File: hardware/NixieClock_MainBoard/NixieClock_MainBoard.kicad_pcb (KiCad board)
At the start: 2 copper layers, 152.4 x 63.5 mm, 107 parts, among them J1 Conn_01x14, J10 Conn_01x04, J11 Conn_01x04, J12 Conn_01x03, J13 Conn_01x03, J2 Conn_01x08, J3 Conn_01x08, J4 Conn_01x08, J5 Conn_01x08, J6 USB_C_Receptacle_USB2.0_16P, J7 Micro_SD_Card, J8 Conn_01x08, J9 Conn_01x03, Q1 BC847, Q2 BC847, Q3 BSS123, Q4 Si2319CDS, U1 ESP32-WROOM-32E, U10 NC7SZ125M5X, U12 NC7SZ125M5X, U13 NC7SZ125M5X, U14 CP2102N-Axx-xQFN24, U15 CH340C, U16 NC7SZ125M5X, U17 NC7SZ125M5X, U18 NC7SZ125M5X, U19 NC7SZ125M5X, U2 R-78C3.3-1.0, U20 NC7SZ125M5X, U21 NC7SZ125M5X, U3 NC7SZ125M5X, U4 PCA9635, U5 NC7SZ125M5X, U6 PCA9538A, U7 NC7SZ125M5X, U8 NC7SZ125M5X, U9 NC7SZ125M5X

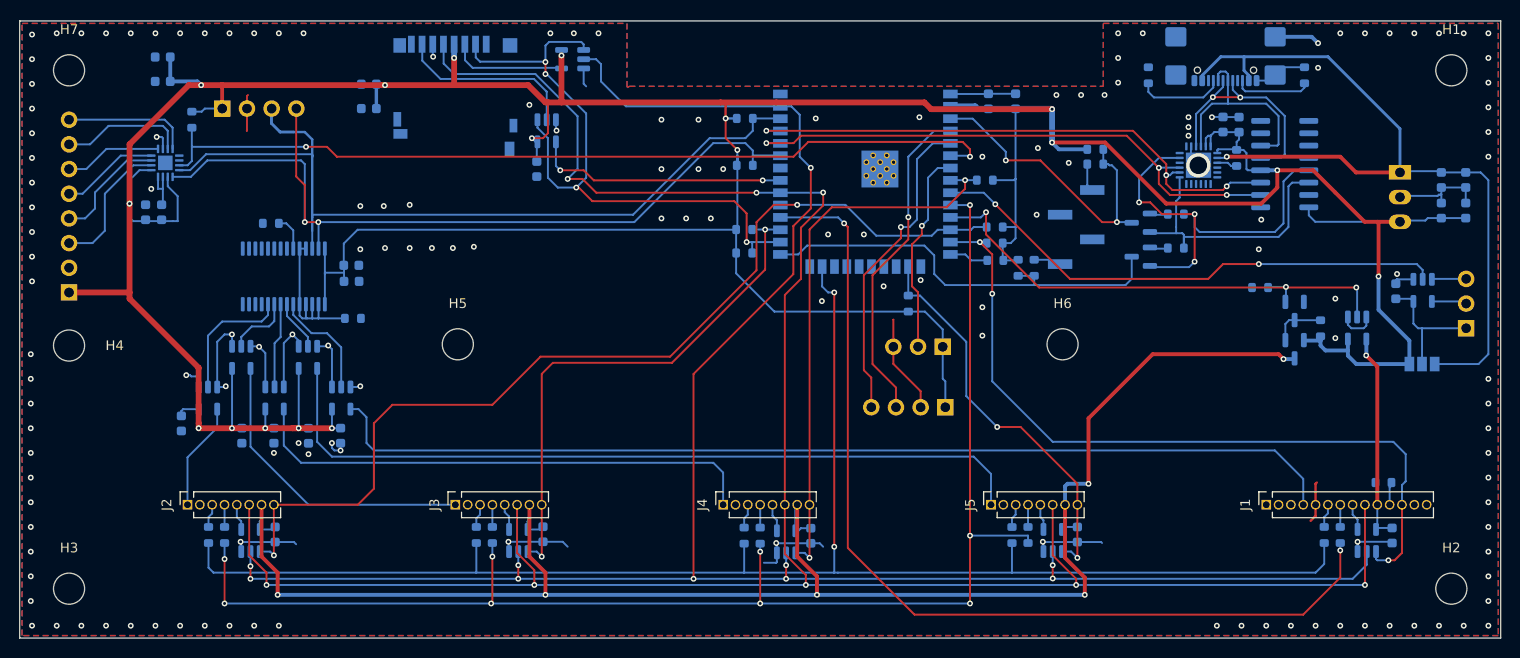
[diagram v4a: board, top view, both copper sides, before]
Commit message: Hardware V2.1 add NixieClock_MainBoard/NixieClock_Schematic.pdf
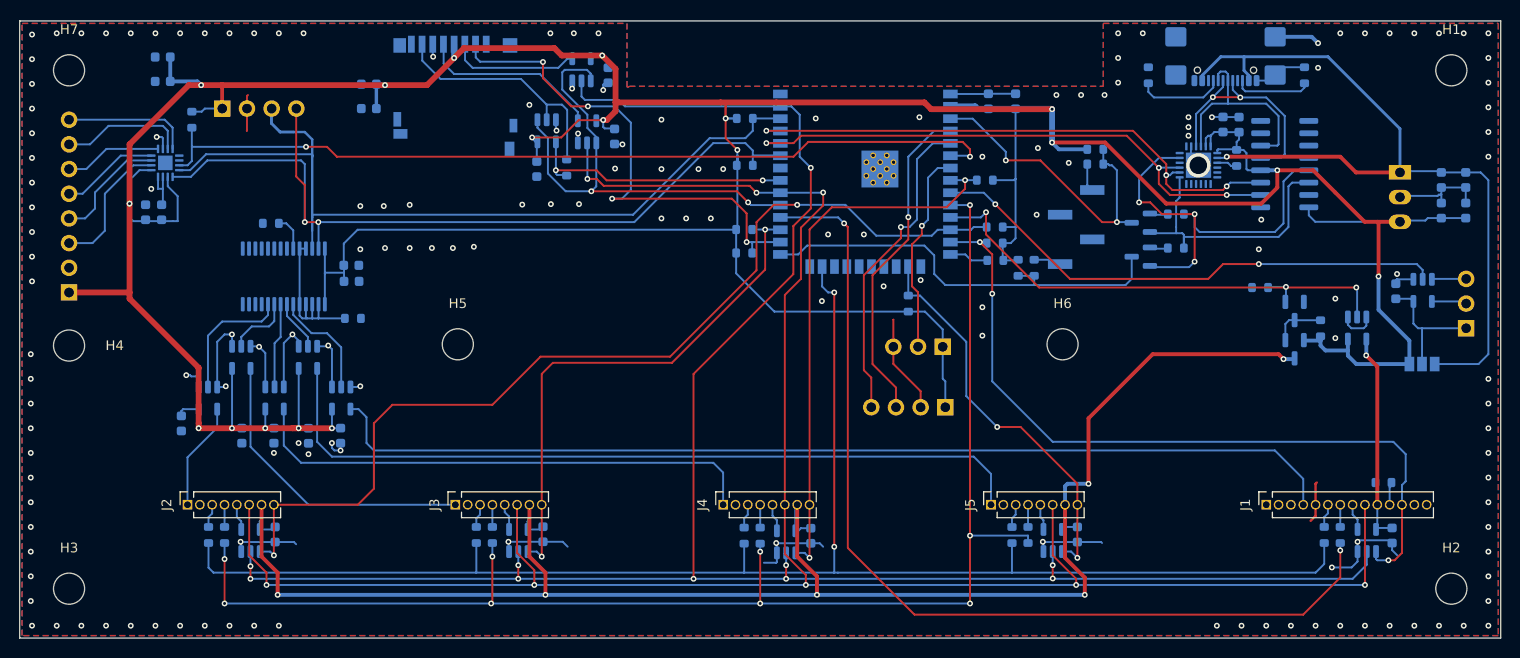
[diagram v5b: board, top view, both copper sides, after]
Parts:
- added C29: 100nF, Capacitor_SMD:C_0603_1608Metric, B.Cu at (98.7, 81.8)
- added C30: 100nF, Capacitor_SMD:C_0603_1608Metric, B.Cu at (99.3, 88.1)
- added R35: R, Resistor_SMD:R_0603_1608Metric, B.Cu at (94.4, 91.3)
- added U11: NC7SZ125M5X, Package_TO_SOT_SMD:SOT-23-5, B.Cu at (96.5, 87.6)
- moved U20 1.42 mm to (95.9, 81.2), turned to 90 degrees
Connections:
- J7 pad 5: /SCLK -> Net-(J7-CLK)
- U1 pad 29: unconnected-(U1-IO5-Pad29) -> /OE_MEM
- U20 pad 1: /CS_MEM_1 -> /OE_MEM
- U21 pad 1: /CS_MEM_1 -> /OE_MEM
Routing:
- net /OE_MEM: track 0.00 -> 49.1 mm, vias 0 -> 2
- net /SCLK: track 243.9 -> 220.0 mm
- net Net-(J7-CLK): track 0.00 -> 19.5 mm
- net /CS_MEM_1: track 66.9 -> 53.3 mm
- net +3.3V: track 479.3 -> 487.6 mm, vias 17 -> 18
- net GND: track 138.7 -> 145.4 mm, vias 152 -> 160
- net Net-(J7-DAT0): track 19.4 -> 26.1 mm
- net Net-(J7-CMD): track 12.0 -> 14.1 mm
- net /MISO: track 26.2 -> 28.0 mm
- net /MOSI: track 206.9 -> 206.1 mm
